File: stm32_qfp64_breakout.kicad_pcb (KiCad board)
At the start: 2 copper layers, 63.5 x 33 mm, 25 parts, among them IC1 NCV8170, J1 Conn_01x24, J2 USB_HS, J3 USB_mini_micro_B, J4 Conn_01x24, J5 SWD, U2 STM32F205RGTx, Y1 8MHz Xtal

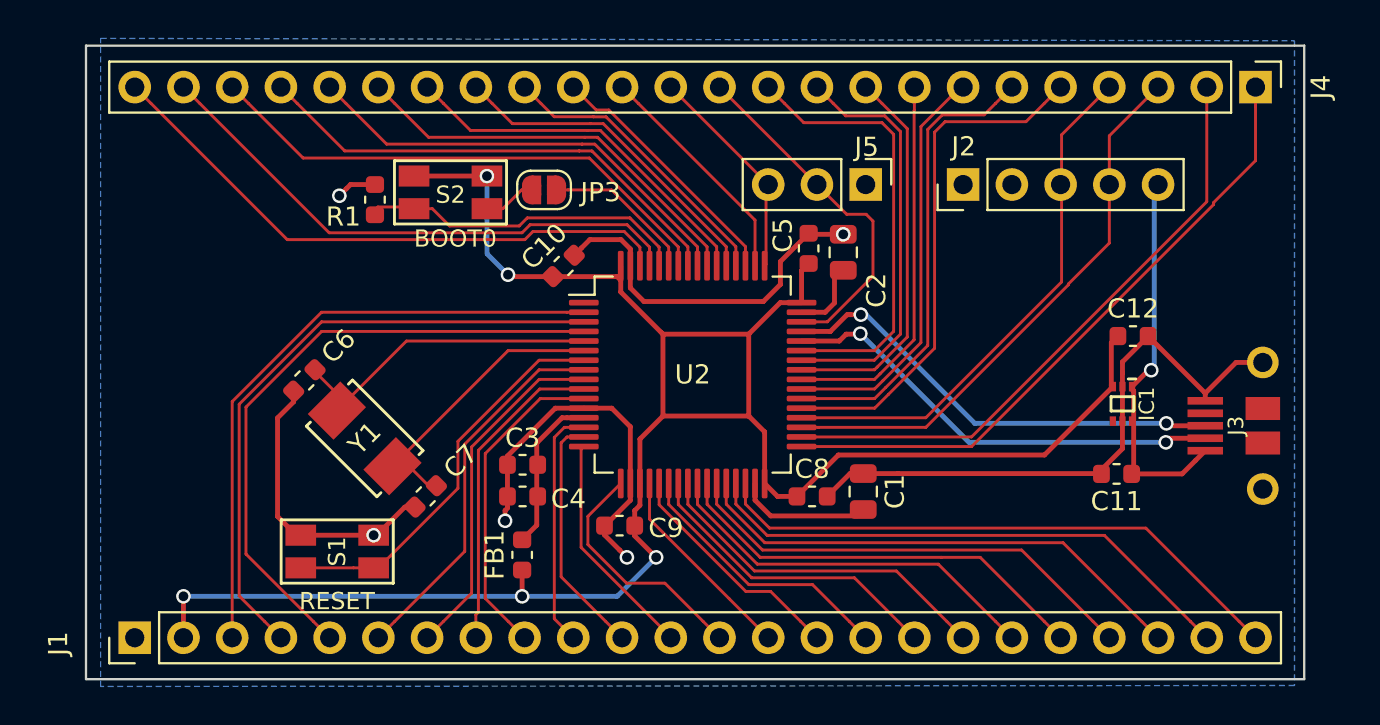
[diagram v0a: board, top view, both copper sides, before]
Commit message: pins are now 0.7 in apart
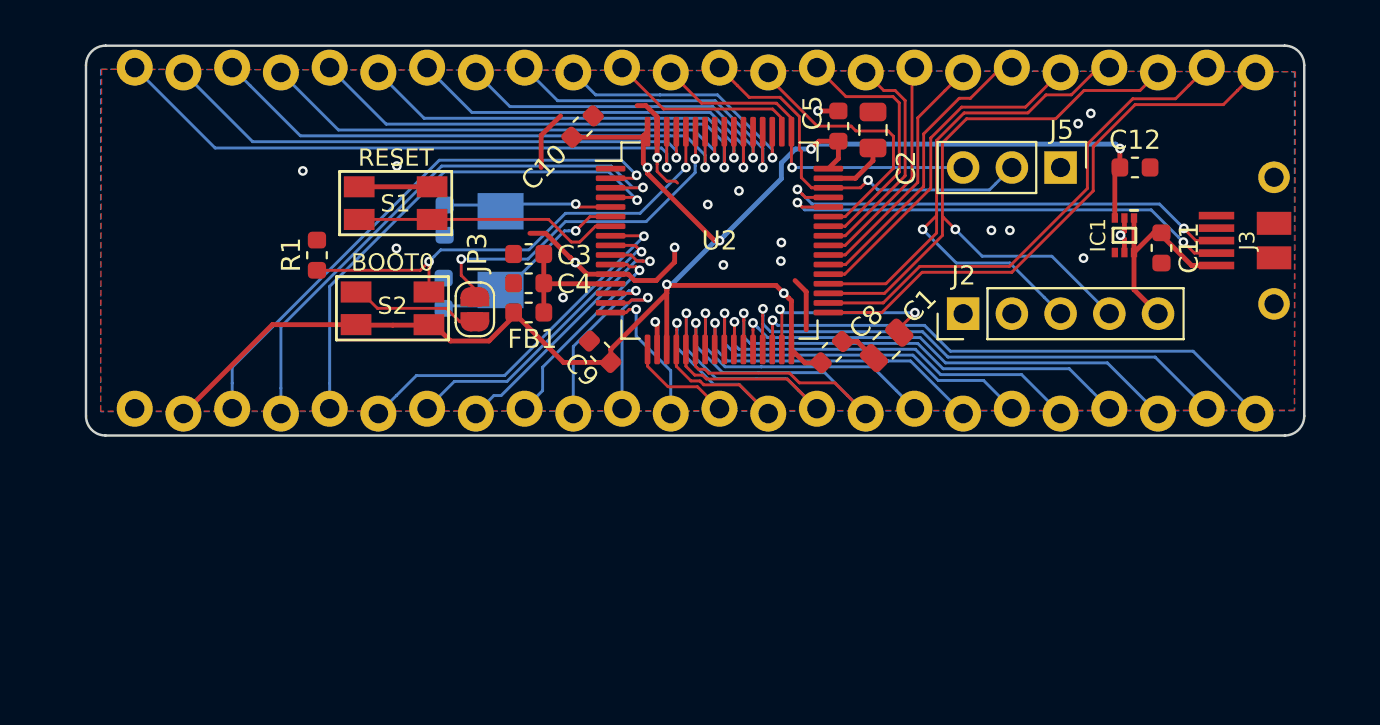
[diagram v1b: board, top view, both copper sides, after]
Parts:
- C6, C7, Y1: moved to B.Cu
- J1, J4: footprint Connector_PinHeader_2.54mm:PinHeader_1x24_P2.54mm_Vertical -> stm32_qfp64_breakout:M24_LOCK_NOSILK
- moved S1 18.4 mm to (105.0, 61.5)
- moved FB1 12.6 mm to (112.0, 67.2), turned to 0 degrees
- moved Y1 12.1 mm to (110.5, 64.0), turned to 270 degrees
- moved C11 12.0 mm to (145.0, 63.9), turned to 270 degrees
- moved J1 11.8 mm to (91.4, 72.4), turned to 0 degrees
- moved C4 11.1 mm to (112.0, 65.7)
- moved C6 11.1 mm to (107.6, 62.4), turned to 270 degrees
- moved C3 11.0 mm to (112.0, 64.2)
- moved C7 10.6 mm to (107.5, 66.2), turned to 90 degrees
- moved J5 10.2 mm to (139.7, 59.7)
- moved J3 9.67 mm to (150.8, 63.5)
- moved C9 9.12 mm to (115.7, 69.3), turned to 135 degrees
- moved C12 8.79 mm to (143.6, 59.7)
- moved IC1 8.79 mm to (143.0, 63.2)
- moved C1 7.71 mm to (130.6, 69.0), turned to 45 degrees
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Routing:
- net GND: track 87.2 -> 31.8 mm, vias 5 -> 20
- net VDD: track 108.2 -> 92.2 mm, vias 5 -> 6
- net B7(BOOT): track 8.06 -> 18.5 mm, vias 0 -> 2
- net VIN: track 20.6 -> 11.0 mm, vias 1 -> 0
- net PA6: track 14.2 -> 23.6 mm, vias 0 -> 1
- net PC6: track 27.0 -> 18.0 mm
- net PA10: track 23.0 -> 14.2 mm
- net PC7: track 24.3 -> 15.4 mm
- net PC8: track 21.5 -> 12.9 mm
- net PC9: track 19.9 -> 11.6 mm
- net PA8: track 20.1 -> 11.9 mm
- net PA5: track 12.2 -> 20.4 mm, vias 0 -> 1
- net PA9: track 21.6 -> 13.5 mm
- net BOOT0: track 16.9 -> 24.9 mm, vias 0 -> 2
- net SWCLK: track 11.4 -> 18.8 mm, vias 0 -> 1
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- added copper zone on F.Cu, net GND
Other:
- board size 63.5 x 33 mm -> 63.5 x 20.3 mm
- net class Power added: clearance 0.1524, trace_width 0.254, via_dia 0.508, via_drill 0.254

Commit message: add microsd slot, refine layout
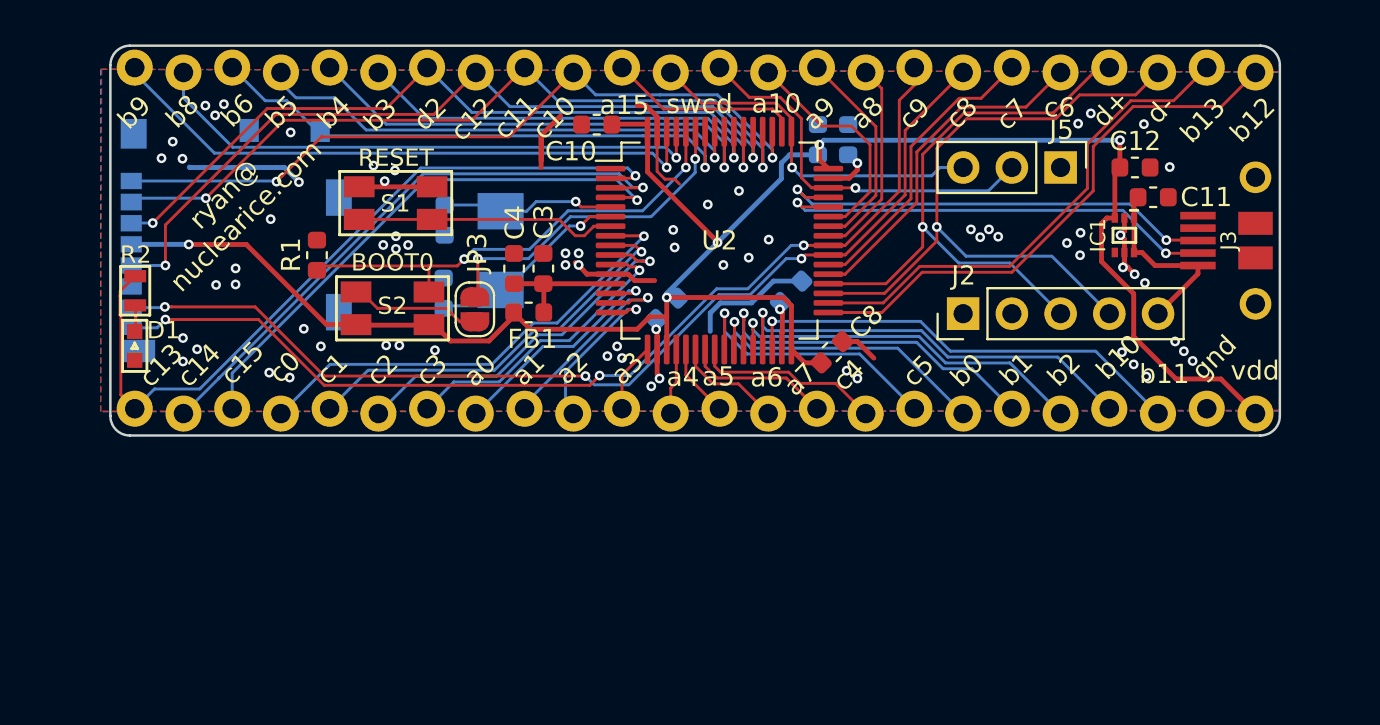
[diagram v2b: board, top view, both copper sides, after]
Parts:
- added D1: LED, flabbergast:LED-0603, F.Cu at (91.4, 69.0)
- added J6: Micro_SD_Card, stm32_qfp64_breakout:MOLEX_104031-0811, B.Cu at (96.5, 63.5)
- added R2: 1kΩ, flabbergast:0603, F.Cu at (91.5, 66.1)
- C1, C2: footprint Capacitor_SMD:C_0805_2012Metric -> Capacitor_SMD:C_0603_1608Metric; moved to B.Cu
- C5, C9: moved to B.Cu
- moved C1 5.71 mm to (125.7, 66.2), turned to 225 degrees
- moved C9 4.14 mm to (119.2, 67.1), turned to 225 degrees
- moved C11 2.68 mm to (144.5, 61.2), turned to 0 degrees
- moved C2 1.39 mm to (128.6, 58.2)
- moved C5 1.28 mm to (127.1, 58.2)
- moved C3 1.08 mm to (112.7, 65.0), turned to 90 degrees
- moved C4 1.08 mm to (111.2, 65.0), turned to 90 degrees
- moved J3 0.97 mm to (149.9, 63.5)
- moved C10 0.74 mm to (115.5, 57.5), turned to 180 degrees
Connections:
- J1 pad 1: GND -> PC13
- J1 pad 10: PA0 -> PA2
- J1 pad 11: PA1 -> PA3
- J1 pad 12: PA2 -> PA4
- J1 pad 13: PA3 -> PA5
- J1 pad 14: PA4 -> PA6
- J1 pad 15: PA5 -> PA7
- J1 pad 16: PA6 -> PC4
- J1 pad 17: PA7 -> PC5
- J1 pad 18: PC4 -> PB0
- J1 pad 19: PC5 -> PB1
- J1 pad 2: VDD -> PC14
- J1 pad 20: PB0 -> PB2
- J1 pad 21: PB1 -> PB10
- J1 pad 22: PB2 -> PB11
- J1 pad 23: PB10 -> GND
- J1 pad 24: PB11 -> VDD
- J1 pad 3: PC13 -> PC15
- J1 pad 4: PC14 -> PC0
- J1 pad 5: PC15 -> PC1
- J1 pad 6: PC0 -> PC2
- J1 pad 7: PC1 -> PC3
- J1 pad 8: PC2 -> PA0
- J1 pad 9: PC3 -> PA1
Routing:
- net PC9: track 11.6 -> 52.8 mm, vias 0 -> 3
- net PC8: track 12.9 -> 54.0 mm, vias 0 -> 3
- net PC10: track 13.8 -> 39.4 mm, vias 1 -> 2
- net PC11: track 17.0 -> 40.7 mm, vias 1 -> 2
- net PC12: track 17.9 -> 41.5 mm, vias 1 -> 2
- net PD2: track 21.2 -> 40.2 mm, vias 1 -> 2
- net PA6: track 23.6 -> 5.69 mm, vias 1 -> 0
- net PA5: track 20.4 -> 3.81 mm, vias 1 -> 0
- net VDD: track 92.2 -> 104.8 mm, vias 6 -> 5
- net PA4: track 15.5 -> 3.46 mm, vias 1 -> 0
- net PC13: track 29.5 -> 40.4 mm
- net Net-(C1-Pad2): track 10.9 -> 2.39 mm, vias 2 -> 1
- net PA7: track 15.9 -> 7.62 mm, vias 1 -> 0
- net GND: track 31.8 -> 39.2 mm, vias 20 -> 69
- net PC4: track 17.0 -> 9.77 mm, vias 1 -> 0
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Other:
- board size 63.5 x 20.3 mm -> 61 x 20.3 mm
- board text added: "a0"
- board text added: "a1"
- board text added: "a10"
- board text added: "a15"
- board text added: "a2"
- board text added: "a3"
- board text added: "a4"
- board text added: "a5"
- board text added: "a6"
- board text added: "a7"
- board text added: "a8"
- board text added: "a9"
- board text added: "b0"
- board text added: "b1"
- board text added: "b10"
- board text added: "b11"
- board text added: "b12"
- board text added: "b13"
- board text added: "b2"
- board text added: "b3"
- board text added: "b4"
- board text added: "b5"
- board text added: "b6"
- board text added: "b8"
- board text added: "b9"
- board text added: "c0"
- board text added: "c1"
- board text added: "c10"
- board text added: "c11"
- board text added: "c12"
- board text added: "c13"
- board text added: "c14"
- board text added: "c15"
- board text added: "c2"
- board text added: "c3"
- board text added: "c4"
- board text added: "c5"
- board text added: "c6"
- board text added: "c7"
- board text added: "c8"
- board text added: "c9"
- board text added: "d+"
- board text added: "d-"
- board text added: "d2"
- board text added: "gnd"
- board text added: "ryan@ nuclearice.com"
- board text added: "swcd"
- board text added: "vdd"
